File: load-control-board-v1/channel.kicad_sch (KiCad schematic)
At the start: 41 parts, among them Q1 AO3400A, Q2 AO3400A, Q3 IRFP7530PBF, U10 OPA188xxDBV, U11 OPA188xxDBV, U12 INA186A1IDCKR

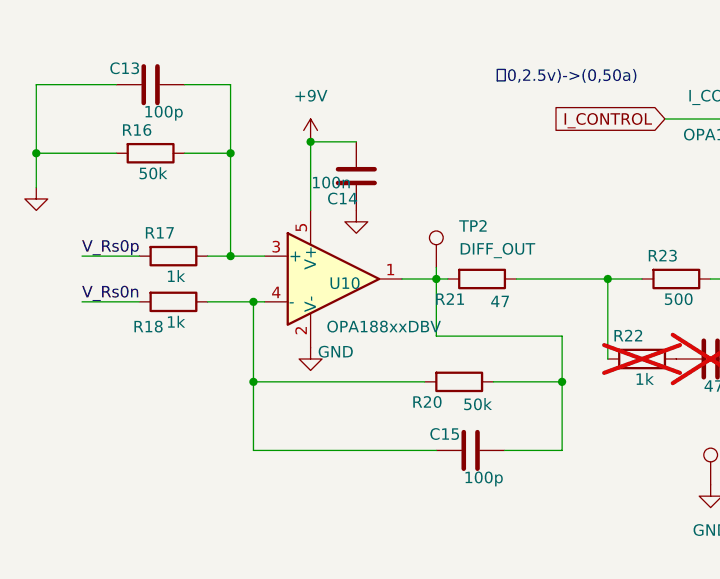
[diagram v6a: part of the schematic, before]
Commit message: Change INA back to 25V/V, change diff gain to 1:40
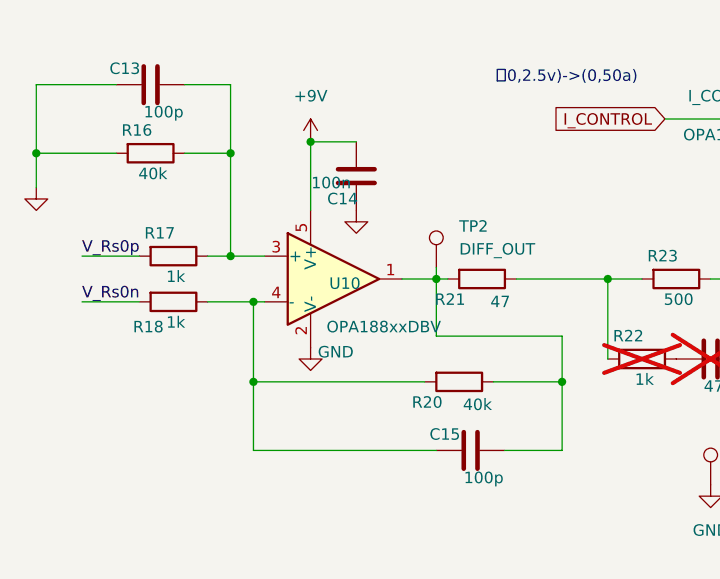
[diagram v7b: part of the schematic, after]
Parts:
- R16, R20: value 50k -> 40k
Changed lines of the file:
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@@
 			)
 		)
-		(property "Value" "50k"
+		(property "Value" "40k"
 			(at 76.962 74.93 90)
 			(effects
@@
 			)
 		)
-		(property "Value" "50k"
+		(property "Value" "40k"
 			(at 40.894 49.276 90)
 			(effects
